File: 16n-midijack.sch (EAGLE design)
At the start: 108 parts, among them J1 PJ302M, J10 PJ302M, J11 PJ302M, J12 PJ302M, J13 PJ302M, J14 PJ302M, J15 PJ302M, J16 PJ302M, J2 PJ302M, J3 PJ302M, J4 PJ302M, J5 PJ302M, J6 PJ302M, J7 PJ302M, J8 PJ302M, J9 PJ302M, U1 MCP6004_SMD, U2 MCP6004_SMD, U3 MCP6004_SMD, U4 MCP6004_SMD, U5 MCP6004_SMD, U6 MCP6004_SMD, U7 MCP6004_SMD, U8 MCP6004_SMD

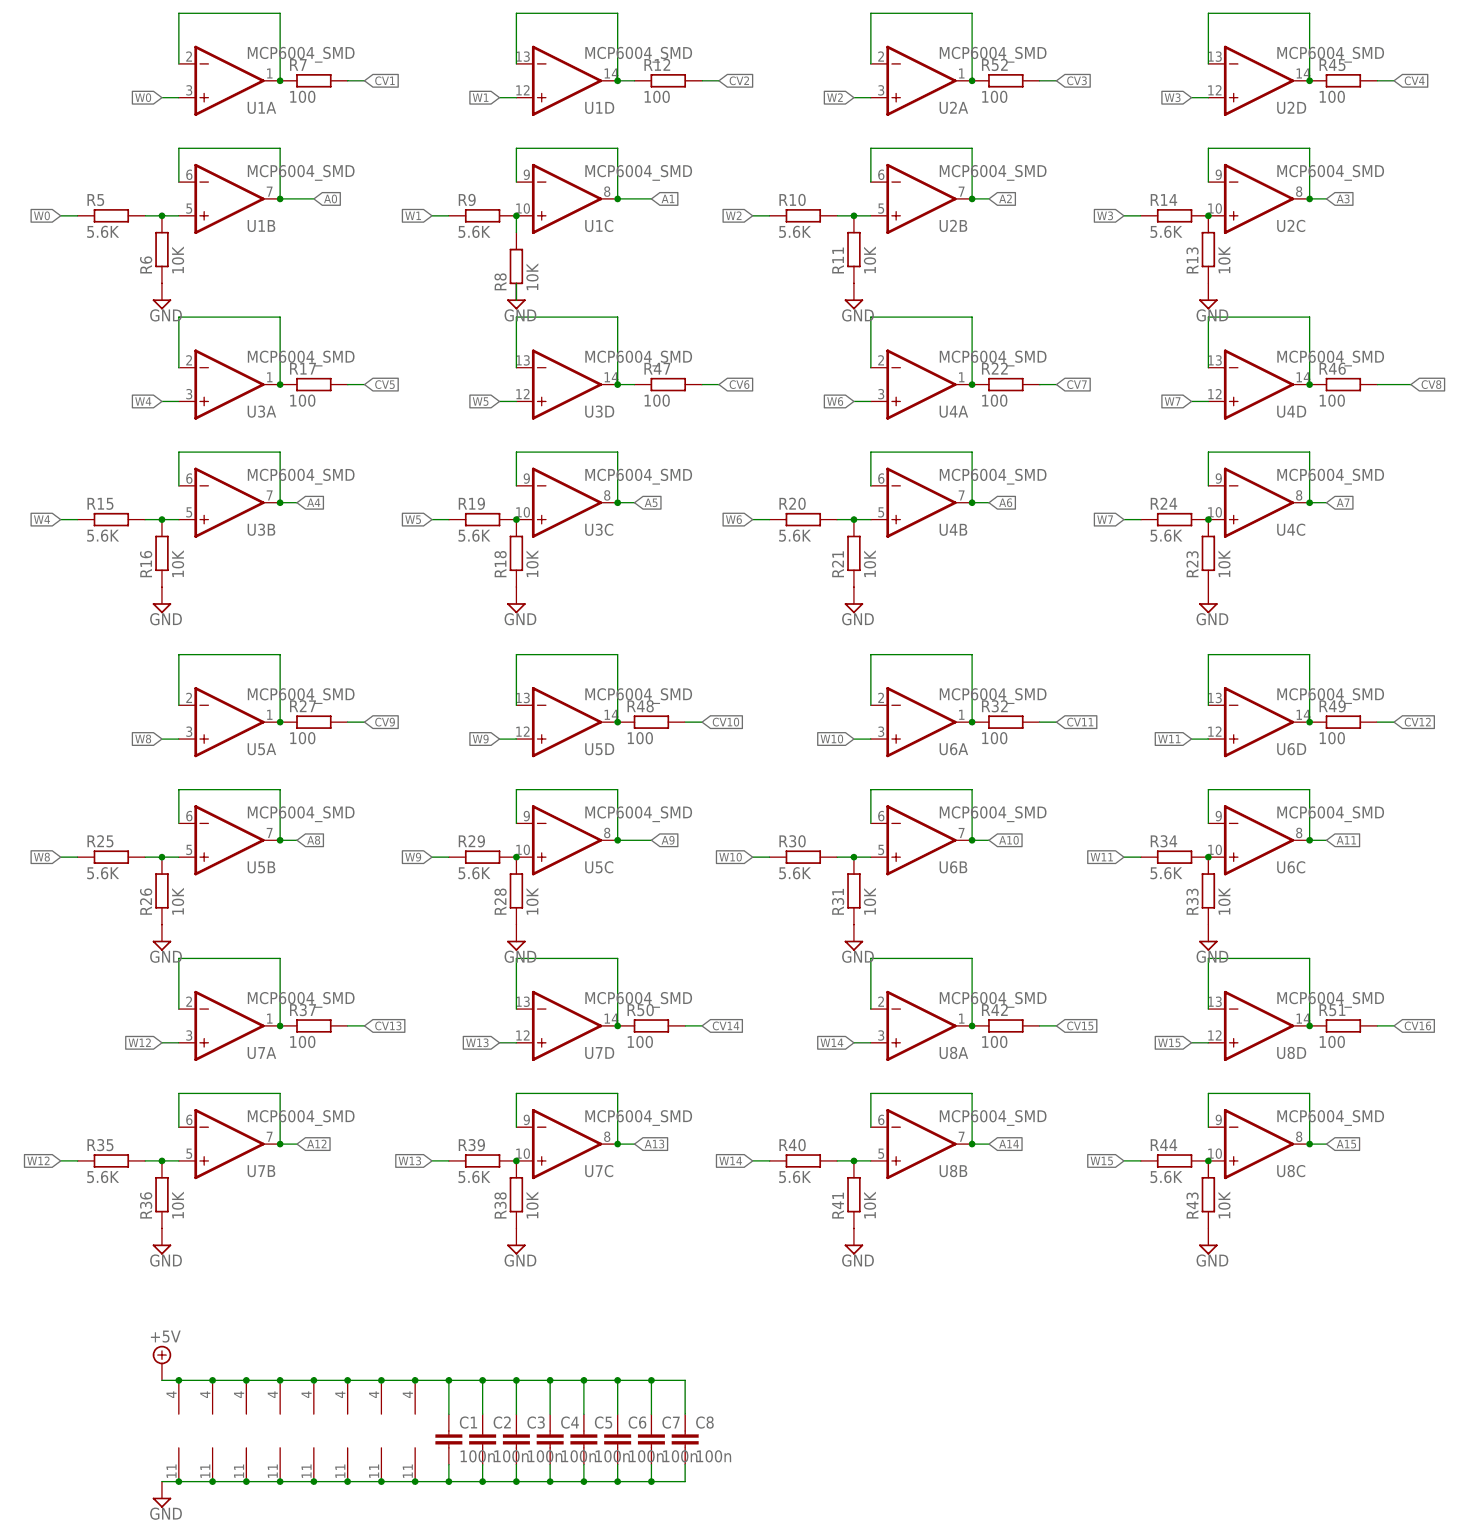
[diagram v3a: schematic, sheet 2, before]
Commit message: Make impedence jacks 1K.
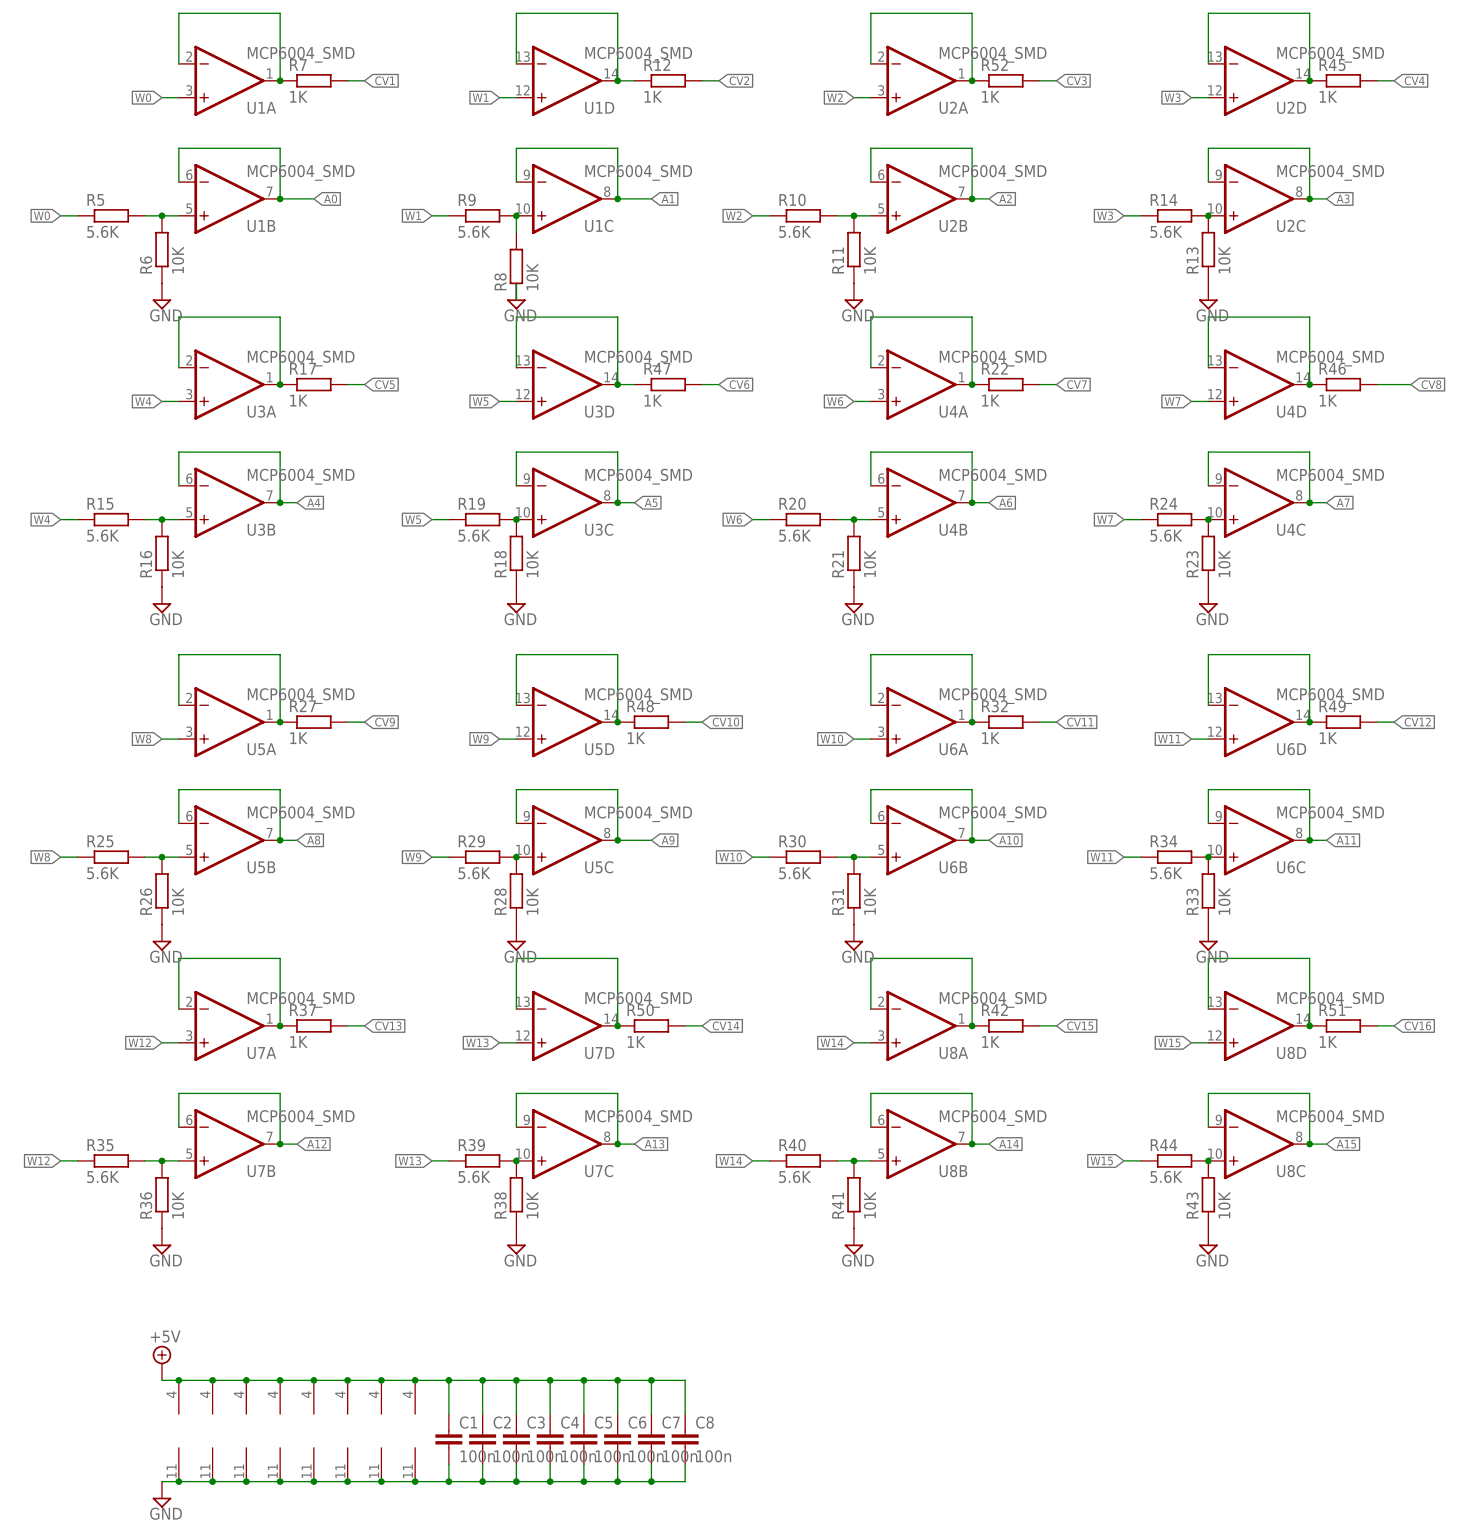
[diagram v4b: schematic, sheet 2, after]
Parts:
- R12, R17, R22, R27, R32, R37, R42, R45, R46, R47, R48, R49, R50, R51, R52, R7: value 100 -> 1K
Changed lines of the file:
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@@
 <part name="R6" library="rcl" library_urn="urn:adsk.eagle:library:334" deviceset="R-EU_" device="R0805" package3d_urn="urn:adsk.eagle:package:23553/2" value="10K"/>
 <part name="SUPPLY34" library="supply2" library_urn="urn:adsk.eagle:library:372" deviceset="GND" device=""/>
-<part name="R7" library="rcl" library_urn="urn:adsk.eagle:library:334" deviceset="R-EU_" device="R0805" package3d_urn="urn:adsk.eagle:package:23553/2" value="100"/>
+<part name="R7" library="rcl" library_urn="urn:adsk.eagle:library:334" deviceset="R-EU_" device="R0805" package3d_urn="urn:adsk.eagle:package:23553/2" value="1K"/>
 <part name="R8" library="rcl" library_urn="urn:adsk.eagle:library:334" deviceset="R-EU_" device="R0805" package3d_urn="urn:adsk.eagle:package:23553/2" value="10K"/>
 <part name="SUPPLY35" library="supply2" library_urn="urn:adsk.eagle:library:372" deviceset="GND" device=""/>
@@
 <part name="R16" library="rcl" library_urn="urn:adsk.eagle:library:334" deviceset="R-EU_" device="R0805" package3d_urn="urn:adsk.eagle:package:23553/2" value="10K"/>
 <part name="SUPPLY38" library="supply2" library_urn="urn:adsk.eagle:library:372" deviceset="GND" device=""/>
-<part name="R17" library="rcl" library_urn="urn:adsk.eagle:library:334" deviceset="R-EU_" device="R0805" package3d_urn="urn:adsk.eagle:package:23553/2" value="100"/>
+<part name="R17" library="rcl" library_urn="urn:adsk.eagle:library:334" deviceset="R-EU_" device="R0805" package3d_urn="urn:adsk.eagle:package:23553/2" value="1K"/>
 <part name="R18" library="rcl" library_urn="urn:adsk.eagle:library:334" deviceset="R-EU_" device="R0805" package3d_urn="urn:adsk.eagle:package:23553/2" value="10K"/>
 <part name="SUPPLY39" library="supply2" library_urn="urn:adsk.eagle:library:372" deviceset="GND" device=""/>
@@
 <part name="R21" library="rcl" library_urn="urn:adsk.eagle:library:334" deviceset="R-EU_" device="R0805" package3d_urn="urn:adsk.eagle:package:23553/2" value="10K"/>
 <part name="SUPPLY40" library="supply2" library_urn="urn:adsk.eagle:library:372" deviceset="GND" device=""/>
-<part name="R22" library="rcl" library_urn="urn:adsk.eagle:library:334" deviceset="R-EU_" device="R0805" package3d_urn="urn:adsk.eagle:package:23553/2" value="100"/>
+<part name="R22" library="rcl" library_urn="urn:adsk.eagle:library:334" deviceset="R-EU_" device="R0805" package3d_urn="urn:adsk.eagle:package:23553/2" value="1K"/>
 <part name="R23" library="rcl" library_urn="urn:adsk.eagle:library:334" deviceset="R-EU_" device="R0805" package3d_urn="urn:adsk.eagle:package:23553/2" value="10K"/>
 <part name="SUPPLY41" library="supply2" library_urn="urn:adsk.eagle:library:372" deviceset="GND" device=""/>
@@
 <part name="R26" library="rcl" library_urn="urn:adsk.eagle:library:334" deviceset="R-EU_" device="R0805" package3d_urn="urn:adsk.eagle:package:23553/2" value="10K"/>
 <part name="SUPPLY42" library="supply2" library_urn="urn:adsk.eagle:library:372" deviceset="GND" device=""/>
-<part name="R27" library="rcl" library_urn="urn:adsk.eagle:library:334" deviceset="R-EU_" device="R0805" package3d_urn="urn:adsk.eagle:package:23553/2" value="100"/>
+<part name="R27" library="rcl" library_urn="urn:adsk.eagle:library:334" deviceset="R-EU_" device="R0805" package3d_urn="urn:adsk.eagle:package:23553/2" value="1K"/>
 <part name="R28" library="rcl" library_urn="urn:adsk.eagle:library:334" deviceset="R-EU_" device="R0805" package3d_urn="urn:adsk.eagle:package:23553/2" value="10K"/>
 <part name="SUPPLY43" library="supply2" library_urn="urn:adsk.eagle:library:372" deviceset="GND" device=""/>
@@
 <part name="R31" library="rcl" library_urn="urn:adsk.eagle:library:334" deviceset="R-EU_" device="R0805" package3d_urn="urn:adsk.eagle:package:23553/2" value="10K"/>
 <part name="SUPPLY44" library="supply2" library_urn="urn:adsk.eagle:library:372" deviceset="GND" device=""/>
-<part name="R32" library="rcl" library_urn="urn:adsk.eagle:library:334" deviceset="R-EU_" device="R0805" package3d_urn="urn:adsk.eagle:package:23553/2" value="100"/>
+<part name="R32" library="rcl" library_urn="urn:adsk.eagle:library:334" deviceset="R-EU_" device="R0805" package3d_urn="urn:adsk.eagle:package:23553/2" value="1K"/>
 <part name="R33" library="rcl" library_urn="urn:adsk.eagle:library:334" deviceset="R-EU_" device="R0805" package3d_urn="urn:adsk.eagle:package:23553/2" value="10K"/>
 <part name="SUPPLY45" library="supply2" library_urn="urn:adsk.eagle:library:372" deviceset="GND" device=""/>
@@
 <part name="R36" library="rcl" library_urn="urn:adsk.eagle:library:334" deviceset="R-EU_" device="R0805" package3d_urn="urn:adsk.eagle:package:23553/2" value="10K"/>
 <part name="SUPPLY46" library="supply2" library_urn="urn:adsk.eagle:library:372" deviceset="GND" device=""/>
-<part name="R37" library="rcl" library_urn="urn:adsk.eagle:library:334" deviceset="R-EU_" device="R0805" package3d_urn="urn:adsk.eagle:package:23553/2" value="100"/>
+<part name="R37" library="rcl" library_urn="urn:adsk.eagle:library:334" deviceset="R-EU_" device="R0805" package3d_urn="urn:adsk.eagle:package:23553/2" value="1K"/>
 <part name="R38" library="rcl" library_urn="urn:adsk.eagle:library:334" deviceset="R-EU_" device="R0805" package3d_urn="urn:adsk.eagle:package:23553/2" value="10K"/>
 <part name="SUPPLY47" library="supply2" library_urn="urn:adsk.eagle:library:372" deviceset="GND" device=""/>
@@
 <part name="R41" library="rcl" library_urn="urn:adsk.eagle:library:334" deviceset="R-EU_" device="R0805" package3d_urn="urn:adsk.eagle:package:23553/2" value="10K"/>
 <part name="SUPPLY48" library="supply2" library_urn="urn:adsk.eagle:library:372" deviceset="GND" device=""/>
-<part name="R42" library="rcl" library_urn="urn:adsk.eagle:library:334" deviceset="R-EU_" device="R0805" package3d_urn="urn:adsk.eagle:package:23553/2" value="100"/>
+<part name="R42" library="rcl" library_urn="urn:adsk.eagle:library:334" deviceset="R-EU_" device="R0805" package3d_urn="urn:adsk.eagle:package:23553/2" value="1K"/>
 <part name="R43" library="rcl" library_urn="urn:adsk.eagle:library:334" deviceset="R-EU_" device="R0805" package3d_urn="urn:adsk.eagle:package:23553/2" value="10K"/>
 <part name="SUPPLY49" library="supply2" library_urn="urn:adsk.eagle:library:372" deviceset="GND" device=""/>
@@
 <part name="C7" library="rcl" library_urn="urn:adsk.eagle:library:334" deviceset="C-EU" device="C0805" package3d_urn="urn:adsk.eagle:package:23617/2" value="100n"/>
 <part name="C8" library="rcl" library_urn="urn:adsk.eagle:library:334" deviceset="C-EU" device="C0805" package3d_urn="urn:adsk.eagle:package:23617/2" value="100n"/>
-<part name="R12" library="rcl" library_urn="urn:adsk.eagle:library:334" deviceset="R-EU_" device="R0805" package3d_urn="urn:adsk.eagle:package:23553/2" value="100"/>
-<part name="R45" library="rcl" library_urn="urn:adsk.eagle:library:334" deviceset="R-EU_" device="R0805" package3d_urn="urn:adsk.eagle:package:23553/2" value="100"/>
-<part name="R46" library="rcl" library_urn="urn:adsk.eagle:library:334" deviceset="R-EU_" device="R0805" package3d_urn="urn:adsk.eagle:package:23553/2" value="100"/>
-<part name="R47" library="rcl" library_urn="urn:adsk.eagle:library:334" deviceset="R-EU_" device="R0805" package3d_urn="urn:adsk.eagle:package:23553/2" value="100"/>
-<part name="R48" library="rcl" library_urn="urn:adsk.eagle:library:334" deviceset="R-EU_" device="R0805" package3d_urn="urn:adsk.eagle:package:23553/2" value="100"/>
-<part name="R49" library="rcl" library_urn="urn:adsk.eagle:library:334" deviceset="R-EU_" device="R0805" package3d_urn="urn:adsk.eagle:package:23553/2" value="100"/>
-<part name="R50" library="rcl" library_urn="urn:adsk.eagle:library:334" deviceset="R-EU_" device="R0805" package3d_urn="urn:adsk.eagle:package:23553/2" value="100"/>
-<part name="R51" library="rcl" library_urn="urn:adsk.eagle:library:334" deviceset="R-EU_" device="R0805" package3d_urn="urn:adsk.eagle:package:23553/2" value="100"/>
-<part name="R52" library="rcl" library_urn="urn:adsk.eagle:library:334" deviceset="R-EU_" device="R0805" package3d_urn="urn:adsk.eagle:package:23553/2" value="100"/>
+<part name="R12" library="rcl" library_urn="urn:adsk.eagle:library:334" deviceset="R-EU_" device="R0805" package3d_urn="urn:adsk.eagle:package:23553/2" value="1K"/>
+<part name="R45" library="rcl" library_urn="urn:adsk.eagle:library:334" deviceset="R-EU_" device="R0805" package3d_urn="urn:adsk.eagle:package:23553/2" value="1K"/>
+<part name="R46" library="rcl" library_urn="urn:adsk.eagle:library:334" deviceset="R-EU_" device="R0805" package3d_urn="urn:adsk.eagle:package:23553/2" value="1K"/>
+<part name="R47" library="rcl" library_urn="urn:adsk.eagle:library:334" deviceset="R-EU_" device="R0805" package3d_urn="urn:adsk.eagle:package:23553/2" value="1K"/>
+<part name="R48" library="rcl" library_urn="urn:adsk.eagle:library:334" deviceset="R-EU_" device="R0805" package3d_urn="urn:adsk.eagle:package:23553/2" value="1K"/>
+<part name="R49" library="rcl" library_urn="urn:adsk.eagle:library:334" deviceset="R-EU_" device="R0805" package3d_urn="urn:adsk.eagle:package:23553/2" value="1K"/>
+<part name="R50" library="rcl" library_urn="urn:adsk.eagle:library:334" deviceset="R-EU_" device="R0805" package3d_urn="urn:adsk.eagle:package:23553/2" value="1K"/>
+<part name="R51" library="rcl" library_urn="urn:adsk.eagle:library:334" deviceset="R-EU_" device="R0805" package3d_urn="urn:adsk.eagle:package:23553/2" value="1K"/>
+<part name="R52" library="rcl" library_urn="urn:adsk.eagle:library:334" deviceset="R-EU_" device="R0805" package3d_urn="urn:adsk.eagle:package:23553/2" value="1K"/>
 <part name="+3V1" library="supply1" deviceset="+3V3" device=""/>
 </parts>
